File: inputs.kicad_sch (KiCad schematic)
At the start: 62 parts, among them J4 TPS43, SW1 KEY_A, SW10 D2F-01F, SW11 RKB2SJM250SMTR, SW12 RKB2SJM250SMTR, SW13 RKB2SJM250SMTR, SW16 D2F-01F, SW17 D2F-01F, SW2 KEY_B, SW3 KEY_C, SW4 KEY_D, SW5 KEY_E, SW6 KEY_F, SW7 D2F-01F, SW8 D2F-01F, SW9 D2F-01F

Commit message: test points
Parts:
- renumbered C32 to C31, C31 to C32, C42 to C35, C43 to C36, C35 to C37, C36 to C38, C37 to C39, R20 to R19, R21 to R20, R25 to R21, R26 to R22, R19 to R24, R22 to R25, R24 to R26, R30 to R29, R29 to R30, R33 to R31, R34 to R32, R47 to R33, R48 to R34, R31 to R35, R32 to R36, R35 to R37, R36 to R38, R49 to R39, R50 to R40, R37 to R41, R39 to R42, R41 to R43, R38 to R44, R40 to R45, R44 to R46, SW16 to SW11, SW17 to SW12, SW11 to SW14, SW12 to SW15

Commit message: new mouse button setup
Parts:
- removed C35, C36: 0.1uF, Capacitor_SMD:C_0805_2012Metric, symbol Device:C
- removed R36, R38, R39, R40: 10k, Resistor_SMD:R_0805_2012Metric, symbol Device:R
- removed SW10, SW11, SW12, SW8: D2F-01F, footprints:D2F01F, symbol user:D2F-01F
- added SW10, SW8: EVQ-Q2H03W, footprints:EVQ-Q2H03W, symbol Switch:SW_Push_Dual
- R32, R34: value 100k -> 10k
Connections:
- net MOUSE_1B is gone; now on net MOUSE_3: C32.1
- net MOUSE_2B is gone; now on net MOUSE_4: C34.1
- net +3V0: no longer R32.1, R34.1
- net GND: now also SW10.1 (1b), SW8.1 (1b)
- net MOUSE_4: now reaches R34.2
- net at R33.2: now also R34.1, SW10.2 (2b)
- net MOUSE_3: now reaches R32.2
- net at R30.2: now also R32.1, SW8.2 (2b)
- net MOUSE_1A renamed MOUSE_1
- net MOUSE_2A renamed MOUSE_2
- no-connect marks 6 -> 2
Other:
- moved on the sheet: C31, C33, C37, C38, C39, J4, MOD2, R29, R31, R35, R37, R41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

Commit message: reannotate
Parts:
- renumbered C33 to C32, C32 to C33, C37 to C35, C38 to C36, C39 to C37, R31 to R30, R30 to R31, R33 to R32, R35 to R33, R37 to R34, R32 to R35, R34 to R36, R41 to R37, R42 to R38, R43 to R39, R44 to R40, R45 to R41, R46 to R42, SW13 to SW11, SW14 to SW12, SW15 to SW13, SW9 to SW8, SW8 to SW9

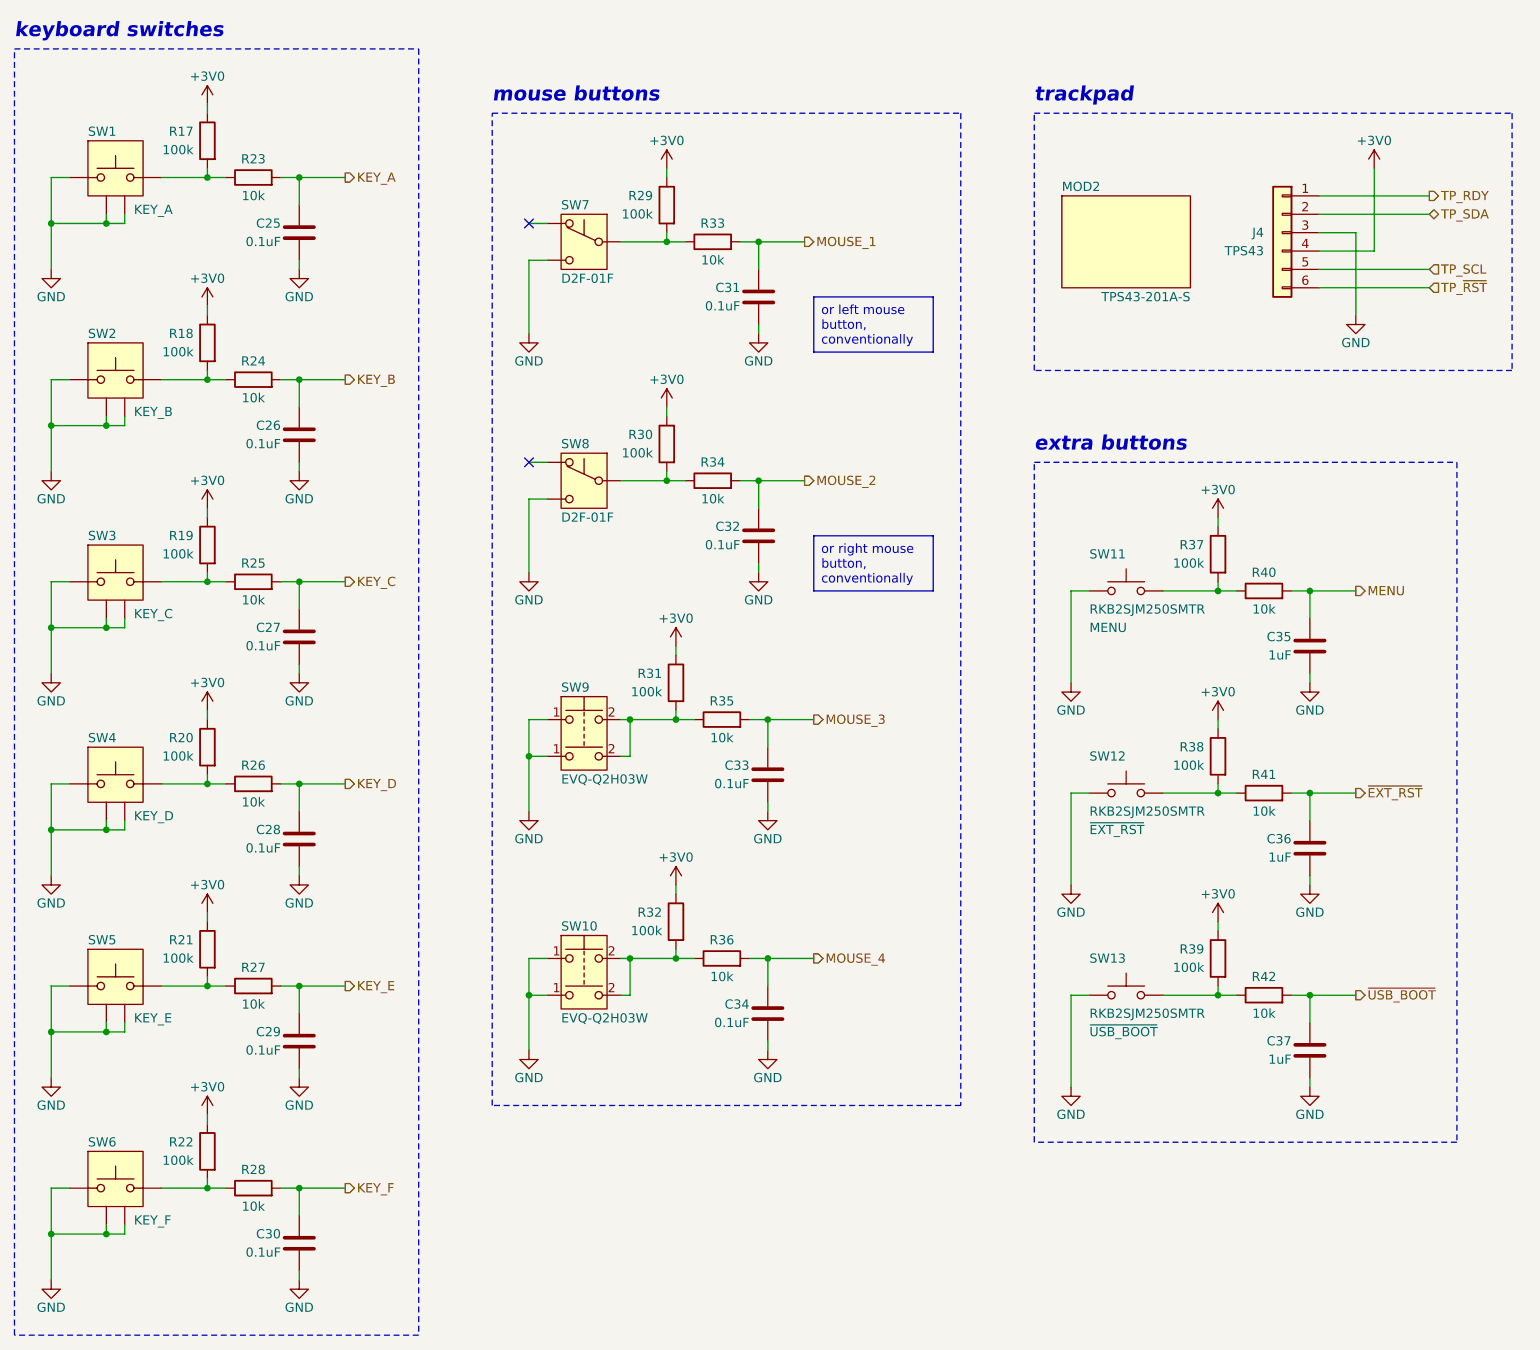
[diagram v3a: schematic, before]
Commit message: use all smd for mouse buttons
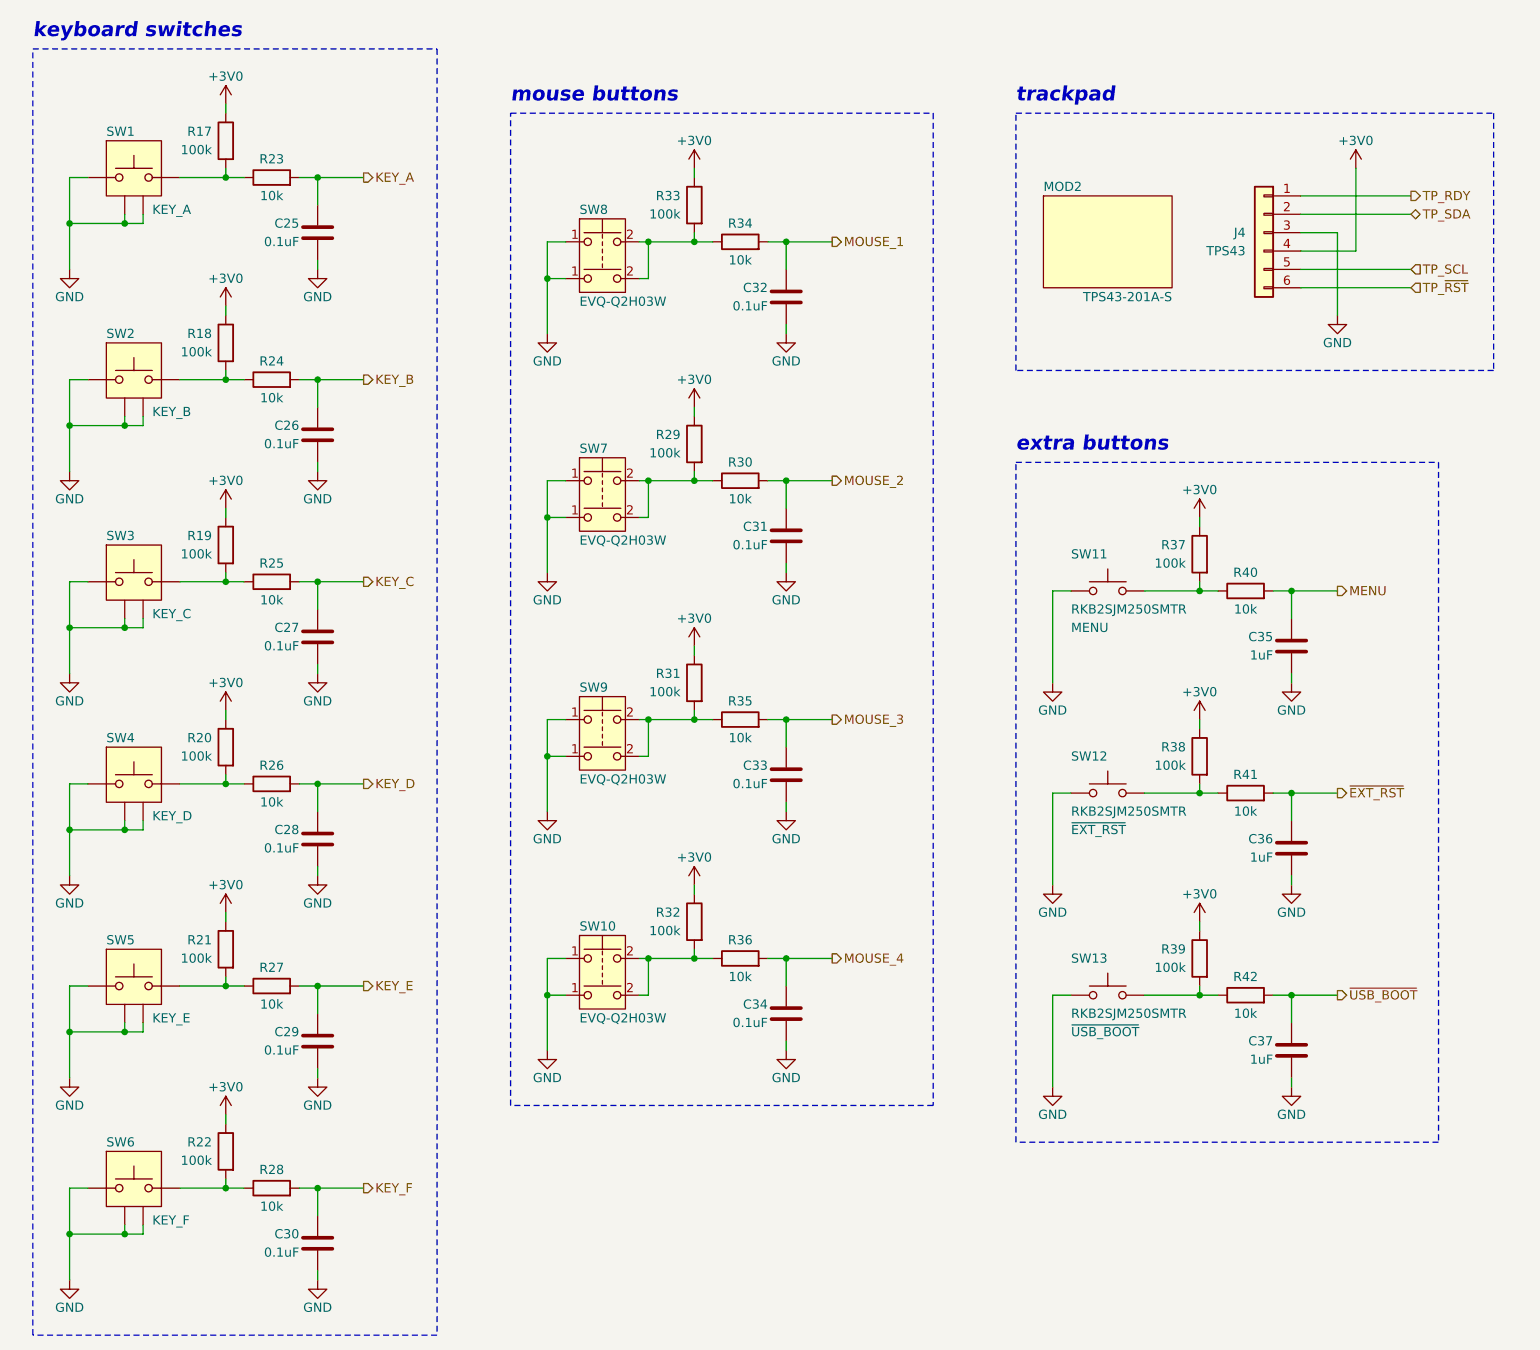
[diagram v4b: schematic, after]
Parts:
- removed SW7, SW8: D2F-01F, footprints:D2F01F, symbol user:D2F-01F
- added SW7, SW8: EVQ-Q2H03W, footprints:EVQ-Q2H03W, symbol Switch:SW_Push_Dual
- R30: value 100k -> 10k
- R33: value 10k -> 100k
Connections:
- net +3V0: now also R33.1; no longer R30.1
- net GND: now also SW7.1 (1b), SW8.1 (1b)
- net MOUSE_1: now also C32.1, R34.2; no longer C31.1, R33.2
- net MOUSE_2: now also C31.1, R30.2; no longer C32.1, R34.2
- net at R29.2: now also R30.1, SW7.2 (2b); no longer R33.1
- net at R34.1: now also R33.2, SW8.2 (2b); no longer R30.2
- no-connect marks 2 -> 0
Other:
- moved on the sheet: C25, C26, C27, C28, C29, C30, C33, C34, C35, C36, C37, J4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

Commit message: reannotate
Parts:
- renumbered C32 to C31, C31 to C32, R33 to R29, R29 to R30, R34 to R33, R30 to R34, SW8 to SW7, SW7 to SW8

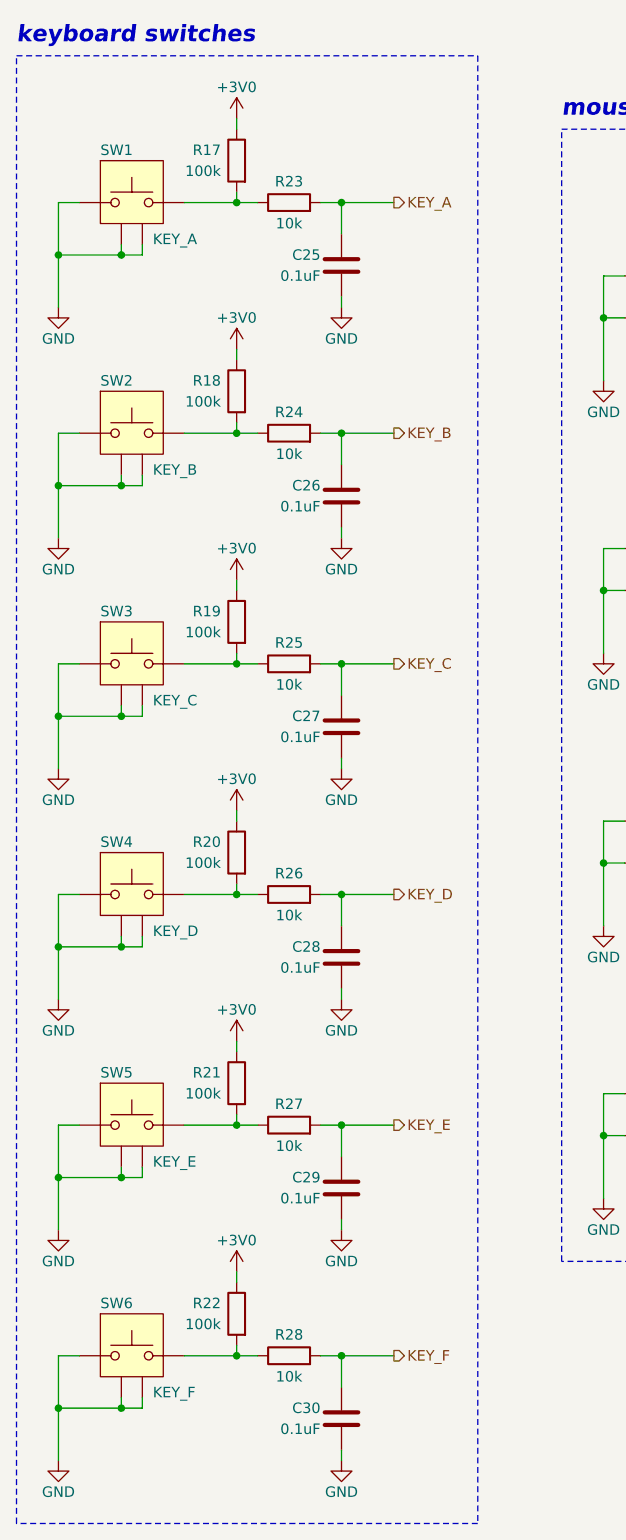
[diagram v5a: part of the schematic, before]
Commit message: move to smd keyboard switches
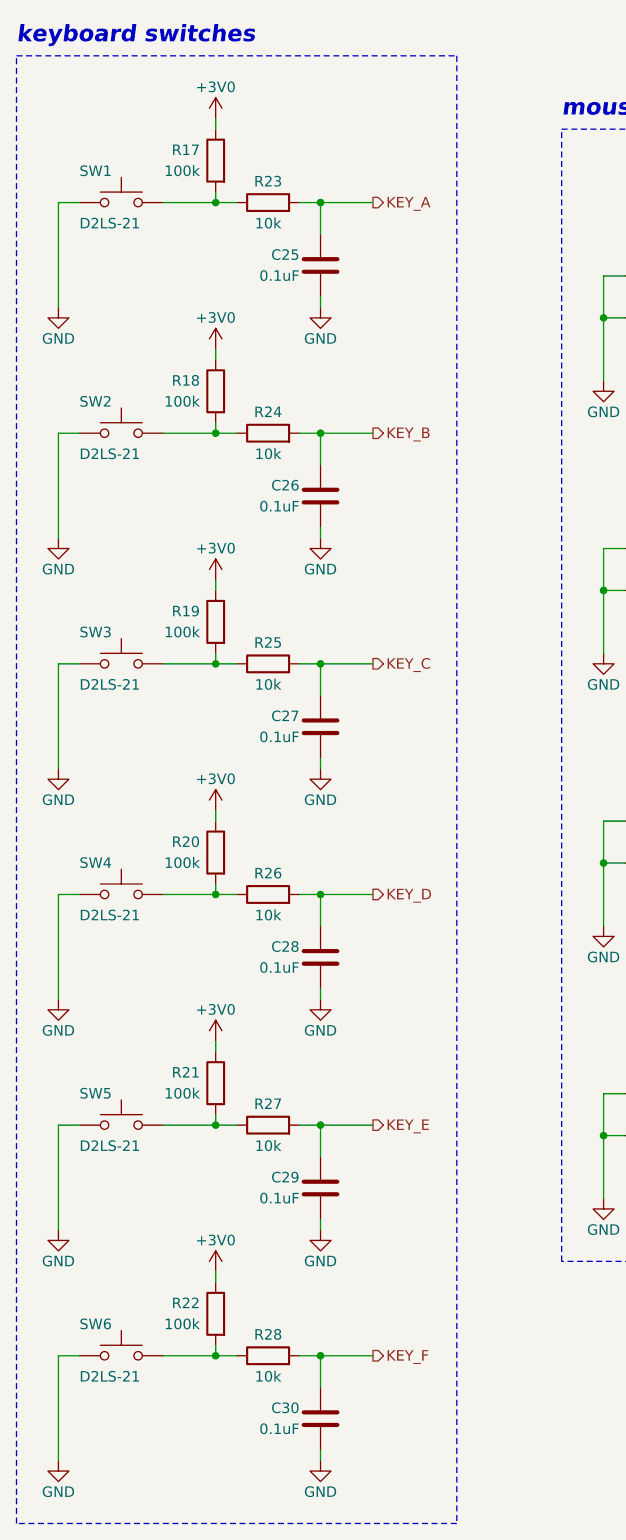
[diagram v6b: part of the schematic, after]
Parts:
- removed SW1: KEY_A, footprints:CPG135001D02, symbol user:Kailh_Choc
- removed SW2: KEY_B, footprints:CPG135001D02, symbol user:Kailh_Choc
- removed SW3: KEY_C, footprints:CPG135001D02, symbol user:Kailh_Choc
- removed SW4: KEY_D, footprints:CPG135001D02, symbol user:Kailh_Choc
- removed SW5: KEY_E, footprints:CPG135001D02, symbol user:Kailh_Choc
- removed SW6: KEY_F, footprints:CPG135001D02, symbol user:Kailh_Choc
- added SW1, SW2, SW3, SW4, SW5, SW6: D2LS-21, footprints:D2LS, symbol Switch:SW_Push
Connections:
- net GND: now also SW1.1, SW2.1, SW3.1, SW4.1, SW5.1, SW6.1
- net at R17.2, R23.1: now also SW1.2
- net at R19.2, R25.1: now also SW3.2
- net at R22.2, R28.1: now also SW6.2
- net at R18.2, R24.1: now also SW2.2
- net at R20.2, R26.1: now also SW4.2
- net at R21.2, R27.1: now also SW5.2
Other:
- moved on the sheet: C25, R17, R23

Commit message: in progress pcb
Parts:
- C25, C26, C27, C28, C29, C30, C31, C32, C33, C34, C35, C36, C37: footprint Capacitor_SMD:C_0805_2012Metric -> Capacitor_SMD:C_0603_1608Metric
- R17, R18, R19, R20, R21, R22, R23, R24, R25, R26, R27, R28, R29, R30, R31, R32, R33, R34, R35, R36, R37, R38, R39, R40, R41, R42: footprint Resistor_SMD:R_0805_2012Metric -> Resistor_SMD:R_0603_1608Metric
